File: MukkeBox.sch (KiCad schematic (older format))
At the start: 44 parts, among them J101 Conn_02x20_Odd_Even, J102 Conn_01x04, J103 Conn_02x05_Odd_Even, J104 Conn_02x05_Odd_Even, U101 LM35-LP, U102 STM32F030C6Tx_MukkeBox, Y101 FOXSDLF/080-20

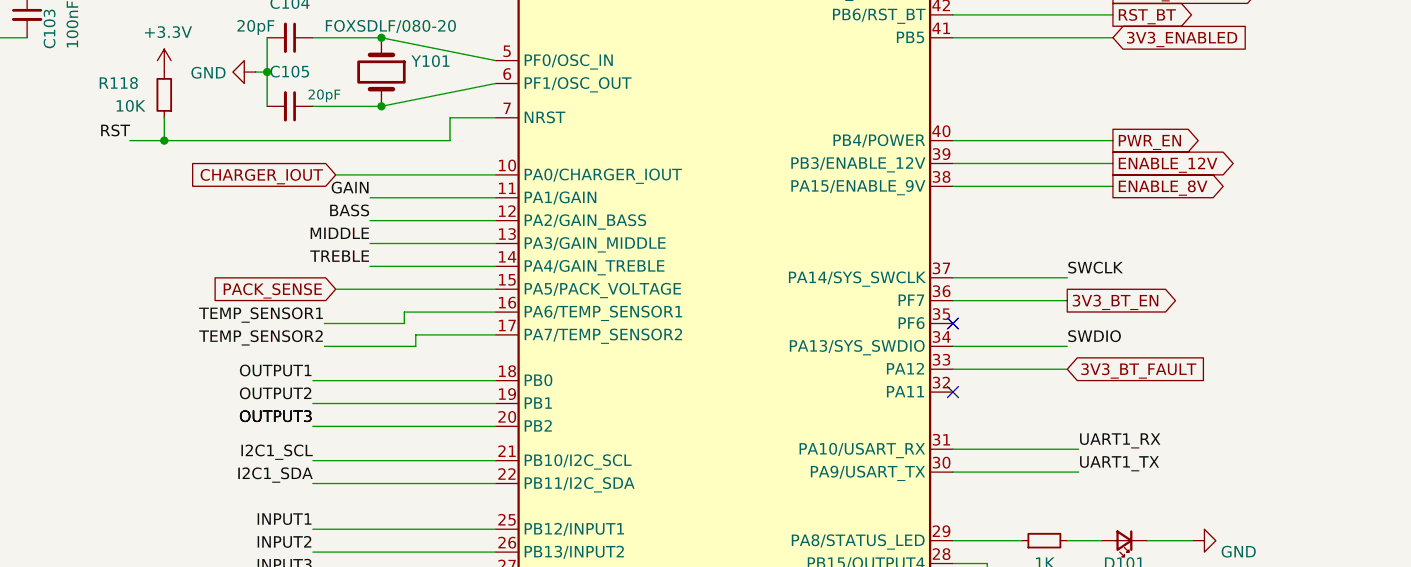
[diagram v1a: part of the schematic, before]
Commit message: Charger ausgetauscht, Mosfet und Dioden durch billigere ersetzt
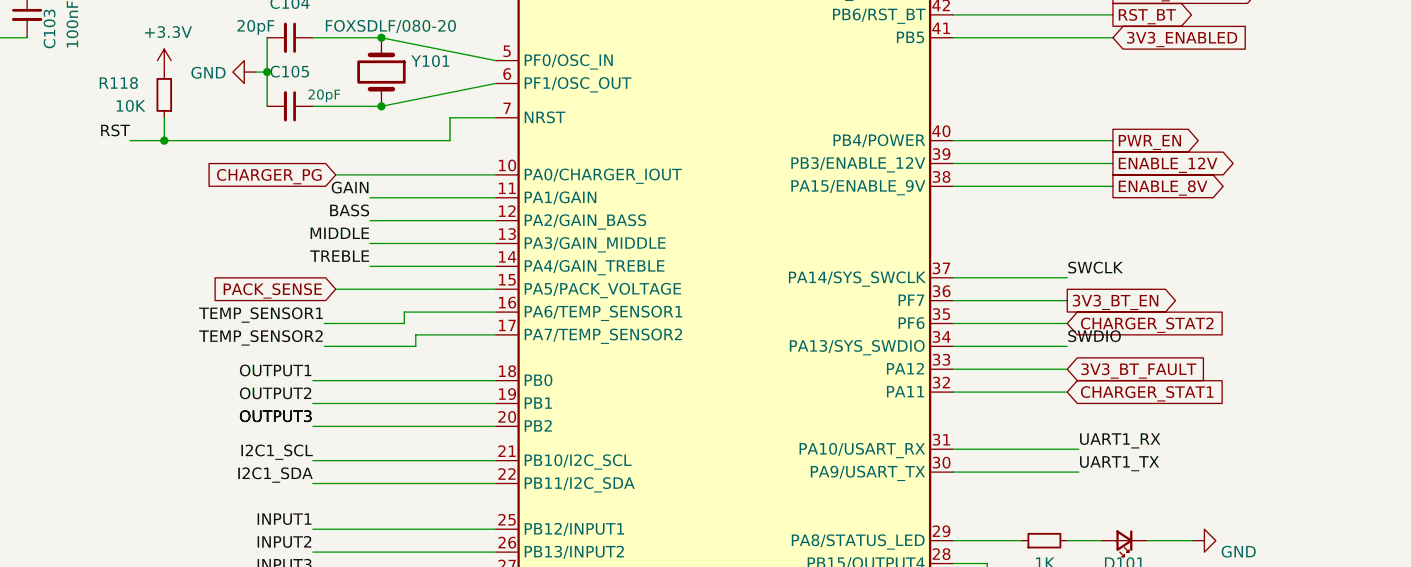
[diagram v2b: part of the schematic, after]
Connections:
- net CHARGER_STAT1: now reaches U102.32 (PA11)
- net CHARGER_STAT2: now reaches U102.35 (PF6)
- net CHARGER_IOUT renamed CHARGER_PG
- no-connect marks 7 -> 5
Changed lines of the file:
@@
 EESchema Schematic File Version 4
-EELAYER 30 0
+LIBS:MukkeBox-cache
+EELAYER 26 0
 EELAYER END
 $Descr A4 11693 8268
@@
 Text GLabel 6300 2750 0    50   Output ~ 0
 CHARGER_DISABLE
-Text GLabel 6300 3750 0    50   Input ~ 0
-CHARGER_IOUT
 Text GLabel 3100 6900 2    50   Input ~ 0
 SCL
@@
 	2850 5400 2650 5400
 NoConn ~ 2650 5500
-NoConn ~ 9000 4700
-NoConn ~ 9000 4400
 $Comp
 L Sensor_Temperature:LM35-LP U101
@@
 Wire Wire Line
 	10150 1200 10150 1600
+Text GLabel 9500 4700 2    50   Input ~ 0
+CHARGER_STAT1
+Wire Wire Line
+	9500 4700 9000 4700
+Text GLabel 9500 4400 2    50   Input ~ 0
+CHARGER_STAT2
+Wire Wire Line
+	9500 4400 9000 4400
+Text GLabel 6300 3750 0    50   Input ~ 0
+CHARGER_PG
 $EndSCHEMATC

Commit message: Änderungen Arbeit hinzugefügt: Layout neuer Charger
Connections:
- net ENABLE_12V: no longer names the net of U102.39 (PB3/ENABLE_12V)
- no-connect marks 5 -> 6
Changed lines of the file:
@@
 EESchema Schematic File Version 4
-LIBS:MukkeBox-cache
-EELAYER 26 0
+EELAYER 30 0
 EELAYER END
 $Descr A4 11693 8268
@@
 	8000 2250 7900 2250
 Wire Wire Line
-	9700 3700 9000 3700
-Wire Wire Line
 	9700 2650 9000 2650
 Wire Wire Line
@@
 Wire Wire Line
 	2000 4600 2150 4600
-Text GLabel 9700 3700 2    50   Output ~ 0
-ENABLE_12V
 Text GLabel 9700 3050 2    50   Output ~ 0
 RST_BT
@@
 Text GLabel 6300 3750 0    50   Input ~ 0
 CHARGER_PG
+NoConn ~ 9000 3700
 $EndSCHEMATC

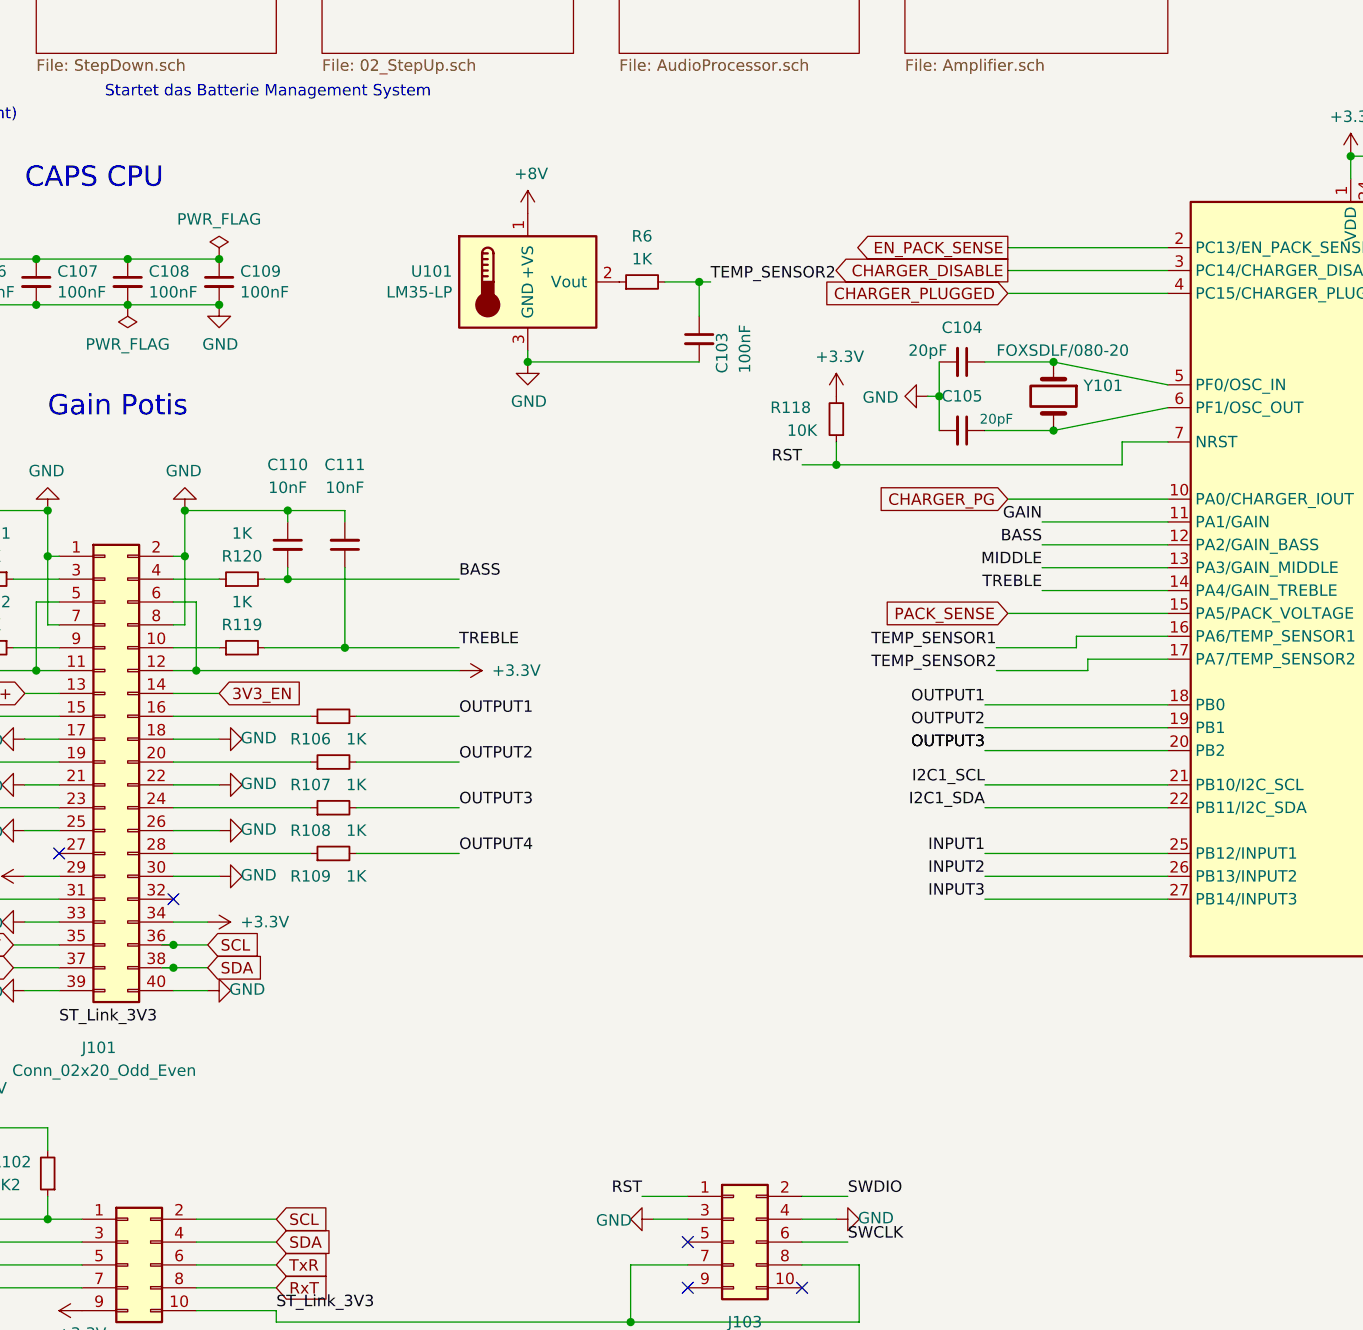
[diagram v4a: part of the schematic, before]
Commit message: Änderungen von der Arbeit, Viele LCSC Teile für teurere ausgetauscht
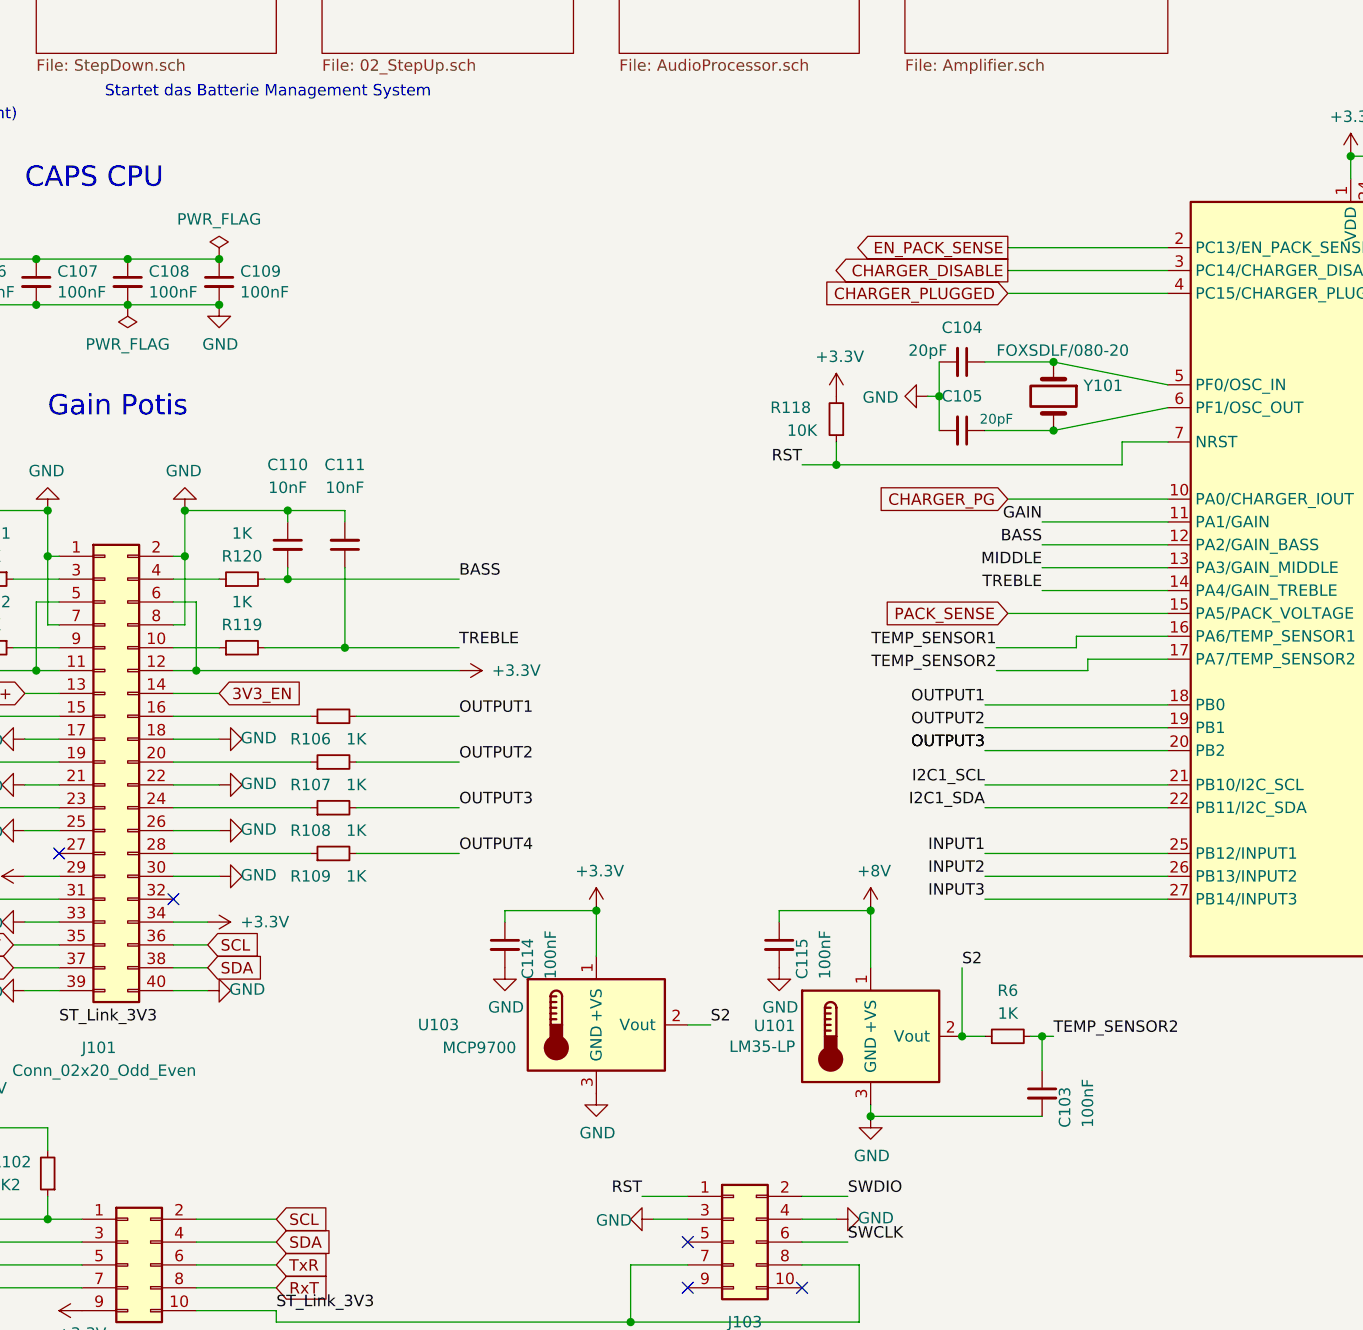
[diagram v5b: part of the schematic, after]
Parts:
- added C114, C115: 100nF, Capacitor_SMD:C_0603_1608Metric_Pad1.05x0.95mm_HandSolder, symbol Device:C_Small
- added U103: MCP9700, Package_TO_SOT_THT:TO-92_Inline, symbol Sensor_Temperature:LM35-LP
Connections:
- net +3V3: now also C114.1, U103.1 (+VS)
- net +8V: now also C115.1
- net GND: now also C114.2, C115.2, U103.3 (GND)
- net S2: now reaches R6.1, U101.2 (Vout)
- net S2: now also U103.2 (Vout)
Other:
- moved on the sheet: C103, R6, U101
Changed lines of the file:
@@
 TxR
-Wire Wire Line
-	2800 5700 2650 5700
-Wire Wire Line
-	2800 5800 2650 5800
 Wire Wire Line
 	2150 5700 1950 5700
@@
 NoConn ~ 4900 7200
 NoConn ~ 4900 7000
-Connection ~ 2650 5700
-Wire Wire Line
-	2650 5700 2600 5700
-Connection ~ 2650 5800
-Wire Wire Line
-	2650 5800 2600 5800
 Wire Wire Line
 	2650 5900 2800 5900
@@
 L Sensor_Temperature:LM35-LP U101
 U 1 1 5FD76FCF
-P 4200 2800
-F 0 "U101" H 3870 2846 50  0000 R CNN
-F 1 "LM35-LP" H 3870 2755 50  0000 R CNN
-F 2 "Package_TO_SOT_THT:TO-92_Inline" H 4250 2550 50  0001 L CNN
-F 3 "http://www.ti.com/lit/ds/symlink/lm35.pdf" H 4200 2800 50  0001 C CNN
-	1    4200 2800
+P 5700 6100
+F 0 "U101" H 5370 6146 50  0000 R CNN
+F 1 "LM35-LP" H 5370 6055 50  0000 R CNN
+F 2 "Package_TO_SOT_THT:TO-92_Inline" H 5750 5850 50  0001 L CNN
+F 3 "http://www.ti.com/lit/ds/symlink/lm35.pdf" H 5700 6100 50  0001 C CNN
+	1    5700 6100
 	1    0    0    -1
 $EndComp
@@
 L power:+8V #PWR0122
 U 1 1 5FD7736F
-P 4200 2500
-F 0 "#PWR0122" H 4200 2350 50  0001 C CNN
-F 1 "+8V" H 4215 2673 50  0000 C CNN
-F 2 "" H 4200 2500 50  0001 C CNN
-F 3 "" H 4200 2500 50  0001 C CNN
-	1    4200 2500
+P 5700 5550
+F 0 "#PWR0122" H 5700 5400 50  0001 C CNN
+F 1 "+8V" H 5715 5723 50  0000 C CNN
+F 2 "" H 5700 5550 50  0001 C CNN
+F 3 "" H 5700 5550 50  0001 C CNN
+	1    5700 5550
 	1    0    0    -1
 $EndComp
@@
 L Device:C_Small C103
 U 1 1 5FD77740
-P 4950 3050
-F 0 "C103" V 5050 2900 50  0000 L CNN
-F 1 "100nF" V 5150 2900 50  0000 L CNN
-F 2 "Capacitor_SMD:C_0603_1608Metric_Pad1.05x0.95mm_HandSolder" H 4950 3050 50  0001 C CNN
-F 3 "~" H 4950 3050 50  0001 C CNN
-	1    4950 3050
-	1    0    0    -1
-$EndComp
-Wire Wire Line
-	4950 2950 4950 2800
-Wire Wire Line
-	4200 3150 4200 3100
+P 6450 6350
+F 0 "C103" V 6550 6200 50  0000 L CNN
+F 1 "100nF" V 6650 6200 50  0000 L CNN
+F 2 "Capacitor_SMD:C_0603_1608Metric_Pad1.05x0.95mm_HandSolder" H 6450 6350 50  0001 C CNN
+F 3 "~" H 6450 6350 50  0001 C CNN
+	1    6450 6350
+	1    0    0    -1
+$EndComp
+Wire Wire Line
+	6450 6250 6450 6100
+Wire Wire Line
+	5700 6450 5700 6400
 $Comp
 L power:GND #PWR0123
 U 1 1 5FD9547D
-P 4200 3150
-F 0 "#PWR0123" H 4200 2900 50  0001 C CNN
-F 1 "GND" H 4205 2977 50  0000 C CNN
-F 2 "" H 4200 3150 50  0001 C CNN
-F 3 "" H 4200 3150 50  0001 C CNN
-	1    4200 3150
-	1    0    0    -1
-$EndComp
-Connection ~ 4200 3150
-Text Label 5000 2800 0    50   ~ 0
+P 5700 6450
+F 0 "#PWR0123" H 5700 6200 50  0001 C CNN
+F 1 "GND" H 5705 6277 50  0000 C CNN
+F 2 "" H 5700 6450 50  0001 C CNN
+F 3 "" H 5700 6450 50  0001 C CNN
+	1    5700 6450
+	1    0    0    -1
+$EndComp
+Connection ~ 5700 6450
+Text Label 6500 6100 0    50   ~ 0
 TEMP_SENSOR2
 Wire Wire Line
-	5000 2800 4950 2800
+	6500 6100 6450 6100
 Text Label 6250 4500 2    50   ~ 0
 TEMP_SENSOR2
@@
 	9700 3150 9000 3150
 Wire Wire Line
-	4200 3150 4950 3150
+	5700 6450 6450 6450
 $Comp
 L Device:R_Small R6
 U 1 1 5EE577C4
-P 4700 2800
-F 0 "R6" V 4900 2800 50  0000 C CNN
-F 1 "1K" V 4800 2800 50  0000 C CNN
-F 2 "Resistor_SMD:R_0603_1608Metric_Pad1.05x0.95mm_HandSolder" H 4700 2800 50  0001 C CNN
-F 3 "~" H 4700 2800 50  0001 C CNN
-	1    4700 2800
-	0    -1   -1   0
-$EndComp
-Wire Wire Line
-	4950 2800 4800 2800
-Connection ~ 4950 2800
+P 6300 6100
+F 0 "R6" V 6500 6100 50  0000 C CNN
+F 1 "1K" V 6400 6100 50  0000 C CNN
+F 2 "Resistor_SMD:R_0603_1608Metric_Pad1.05x0.95mm_HandSolder" H 6300 6100 50  0001 C CNN
+F 3 "~" H 6300 6100 50  0001 C CNN
+	1    6300 6100
+	0    -1   -1   0
+$EndComp
+Wire Wire Line
+	6450 6100 6400 6100
+Connection ~ 6450 6100
 Text GLabel 9500 4300 2    50   Output ~ 0
 3V3_BT_EN
@@
 CHARGER_PG
 NoConn ~ 9000 3700
+Wire Wire Line
+	2800 5700 2650 5700
+Wire Wire Line
+	2650 5800 2800 5800
+$Comp
+L Sensor_Temperature:LM35-LP U103
+U 1 1 5EFDBF70
+P 4500 6050
+F 0 "U103" H 3900 6050 50  0000 R CNN
+F 1 "MCP9700" H 4150 5950 50  0000 R CNN
+F 2 "Package_TO_SOT_THT:TO-92_Inline" H 4550 5800 50  0001 L CNN
+F 3 "http://www.ti.com/lit/ds/symlink/lm35.pdf" H 4500 6050 50  0001 C CNN
+	1    4500 6050
+	1    0    0    -1
+$EndComp
+$Comp
+L power:GND #PWR0134
+U 1 1 5EFDD718
+P 4500 6350
+F 0 "#PWR0134" H 4500 6100 50  0001 C CNN
+F 1 "GND" H 4505 6177 50  0000 C CNN
+F 2 "" H 4500 6350 50  0001 C CNN
+F 3 "" H 4500 6350 50  0001 C CNN
+	1    4500 6350
+	1    0    0    -1
+$EndComp
+$Comp
+L power:+3.3V #PWR0133
+U 1 1 5EFDDB56
+P 4500 5550
+F 0 "#PWR0133" H 4500 5400 50  0001 C CNN
+F 1 "+3.3V" H 4515 5723 50  0000 C CNN
+F 2 "" H 4500 5550 50  0001 C CNN
+F 3 "" H 4500 5550 50  0001 C CNN
+	1    4500 5550
+	1    0    0    -1
+$EndComp
+Wire Wire Line
+	6100 6100 6100 5800
+Wire Wire Line
+	5000 6050 4900 6050
+Wire Wire Line
+	6200 6100 6100 6100
+Connection ~ 6100 6100
+Text Label 6100 5800 0    50   ~ 0
+S2
+Text Label 5000 6050 0    50   ~ 0
+S2
+$Comp
+L Device:C_Small C115
+U 1 1 5F0749E6
+P 5300 5700
+F 0 "C115" V 5400 5550 50  0000 L CNN
+F 1 "100nF" V 5500 5550 50  0000 L CNN
+F 2 "Capacitor_SMD:C_0603_1608Metric_Pad1.05x0.95mm_HandSolder" H 5300 5700 50  0001 C CNN
+F 3 "~" H 5300 5700 50  0001 C CNN
+	1    5300 5700
+	1    0    0    -1
+$EndComp
+$Comp
+L Device:C_Small C114
+U 1 1 5F074EDC
+P 4100 5700
+F 0 "C114" V 4200 5550 50  0000 L CNN
+F 1 "100nF" V 4300 5550 50  0000 L CNN
+F 2 "Capacitor_SMD:C_0603_1608Metric_Pad1.05x0.95mm_HandSolder" H 4100 5700 50  0001 C CNN
+F 3 "~" H 4100 5700 50  0001 C CNN
+	1    4100 5700
+	1    0    0    -1
+$EndComp
+Wire Wire Line
+	4500 5550 4100 5550
+Wire Wire Line
+	4100 5550 4100 5600
+Wire Wire Line
+	4500 5550 4500 5750
+Connection ~ 4500 5550
+Wire Wire Line
+	5700 5550 5700 5800
+Wire Wire Line
+	5300 5600 5300 5550
+Wire Wire Line
+	5300 5550 5700 5550
+Connection ~ 5700 5550
+$Comp
+L power:GND #PWR0135
+U 1 1 5F0B7A70
+P 5300 5800
+F 0 "#PWR0135" H 5300 5550 50  0001 C CNN
+F 1 "GND" H 5305 5627 50  0000 C CNN
+F 2 "" H 5300 5800 50  0001 C CNN
+F 3 "" H 5300 5800 50  0001 C CNN
+	1    5300 5800
+	1    0    0    -1
+$EndComp
+$Comp
+L power:GND #PWR0132
+U 1 1 5F0B7D6E
+P 4100 5800
+F 0 "#PWR0132" H 4100 5550 50  0001 C CNN
+F 1 "GND" H 4105 5627 50  0000 C CNN
+F 2 "" H 4100 5800 50  0001 C CNN
+F 3 "" H 4100 5800 50  0001 C CNN
+	1    4100 5800
+	1    0    0    -1
+$EndComp
 $EndSCHEMATC

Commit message: Fast fertig TODO: Connector umverdrahten mit beschriftung
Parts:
- C101, C102, C103, C106, C107, C108, C109, C114, C115: value 100nF -> 100n
- C104, C105: value 20pF -> 20p
- C110, C111, C112, C113: value 10nF -> 10n
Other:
- note removed: "Charging Current\n (max. 4V entspricht 200mV Shunt)"
- note removed: "Startet das Batterie Management System"
- moved on the sheet: C106, C107, C108, C109, H105, J104, R101, R102
